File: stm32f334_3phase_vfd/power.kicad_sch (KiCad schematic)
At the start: 4 parts, among them U201 STGIB15CH60TS-L, U202 CC6903SO-x0A, U203 CC6903SO-x0A, U204 CC6903SO-x0A

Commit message: continue schematic work
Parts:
- added C201, C202, C203: 4.7u, symbol Device:C_Small
- added C? (x6): 10p, Capacitor_SMD:C_1206_3216Metric, symbol Device:C_Small
- added C? (x2): 4.7u, Capacitor_SMD:C_1206_3216Metric, symbol Device:C_Small
- added C? (x5): 100n, Capacitor_SMD:C_1206_3216Metric, symbol Device:C_Small
- added C?: 330p, Capacitor_SMD:C_1206_3216Metric, symbol Device:C_Small
- added C?: 1n, Capacitor_SMD:C_1206_3216Metric, symbol Device:C_Small
- added C?: 100n/600V, Capacitor_SMD:C_1206_3216Metric, symbol Device:C_Small
- added J201: TP01, symbol Connector_Generic:Conn_01x01
- added J202: TP02, symbol Connector_Generic:Conn_01x01
- added J203: TP03, symbol Connector_Generic:Conn_01x01
- added J? (x4): TP04, symbol Connector_Generic:Conn_01x01
- added R?: 0.050, symbol Device:R_Small
- added R? (x2): 10k, symbol Device:R_Small
- added R? (x6): 1k, Resistor_SMD:R_1206_3216Metric, symbol Device:R_Small
- added R? (x6): 10k, Resistor_SMD:R_1206_3216Metric, symbol Device:R_Small
- added R?: 1k, symbol Device:R_Small
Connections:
- net at U203.1 (IP+): now also U201.22 (V), U203.2 (IP+), C202.1, J?.1 (Pin_1)
- net OUTPUT_PHB: now reaches U203.3 (IP-)
- net OUTPUT_PHB: now also U203.4 (IP-)
- net GND: now reaches U203.5 (GND)
- net GND: now also U201.16 (GND), U201.9 (GND), U202.5 (GND), U204.5 (GND), C?.1, C?.1, C?.1, C?.1, C?.2, C?.2, C?.2, C?.2, C?.2, C?.2, C?.2, C?.2, C?.2, C?.2, C?.2, C?.2, R?.2, R?.2, R?.2, R?.2, R?.2, R?.2, R?.2, R?.2
- net I_B: now reaches U203.7 (OUT)
- net 3V3_ISENS: now reaches U203.8 (VCC)
- net 3V3_ISENS: now also U202.8 (VCC), U204.8 (VCC), C?.2, C?.2, C?.2
- net lin_u: now reaches U201.10 (LinU)
- net lin_u: now also C?.1, R?.2
- net lin_v: now reaches U201.11 (LinV)
- net lin_v: now also C?.1, R?.2
- net lin_w: now reaches U201.12 (LinW)
- net lin_w: now also C?.1, R?.2
- net VCC_15V: now reaches U201.13 (VccL)
- net VCC_15V: now also U201.8 (VccH), C?.1, C?.1, C?.1, C?.1
- net EM_STOP: now reaches U201.14 (~{SD}/OD)
- net EM_STOP: now also C?.1, R?.1
- net Cin: now reaches U201.15 (Cin)
- net Cin: now also C?.1, J?.1 (Pin_1), R?.1, R?.1
- net Tso: now reaches U201.17 (TSO)
- net N: now reaches U201.18 (NW)
- net N: now also U201.19 (NV), U201.20 (NU), R?.1, R?.2
- net at U201.2 (VbootU): now also C201.2, J201.1 (Pin_1)
- net at U201.21 (W): now also U204.1 (IP+), U204.2 (IP+), C203.1, J?.1 (Pin_1)
- net at U201.23 (U): now also U202.1 (IP+), U202.2 (IP+), C201.1, J?.1 (Pin_1)
- net HV: now reaches U201.24 (P)
- net HV: now also C?.2
- net T2: now reaches U201.25 (T2)
- net T1: now reaches U201.26 (T1)
- net at U201.3 (VbootV): now also C202.2, J202.1 (Pin_1)
- net at U201.4 (VbootW): now also C203.2, J203.1 (Pin_1)
- net hin_u: now reaches U201.5 (HinU)
- net hin_u: now also C?.1, R?.2
- net hin_v: now reaches U201.6 (HinV)
- net hin_v: now also C?.1, R?.2
- net hin_w: now reaches U201.7 (HinW)
- net hin_w: now also C?.1, R?.2
- net OUTPUT_PHC: now reaches U204.3 (IP-)
- net OUTPUT_PHC: now also U204.4 (IP-)
- net I_C: now reaches U204.7 (OUT)
- net OUTPUT_PHA: now reaches U202.3 (IP-)
- net OUTPUT_PHA: now also U202.4 (IP-)
- net I_A: now reaches U202.7 (OUT)
- new net 3V3_DIG: R?.2
- new net HinU: R?.1, R?.1
- new net HinV: R?.1, R?.1
- new net HinW: R?.1, R?.1
- new net LinU: R?.1, R?.1
- new net LinV: R?.1, R?.1
- new net LinW: R?.1, R?.1
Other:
- moved on the sheet: U201, U202, U203, U204

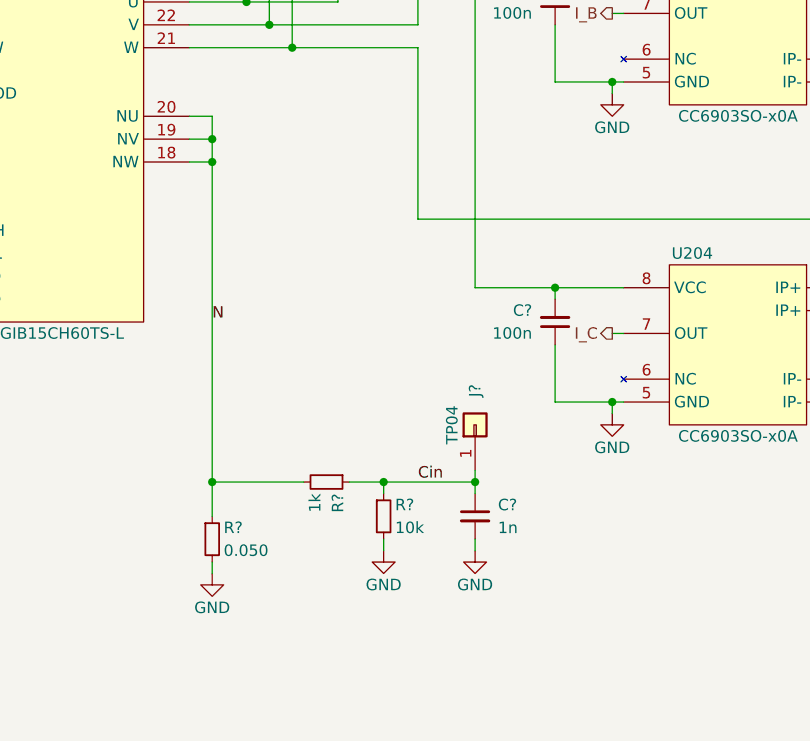
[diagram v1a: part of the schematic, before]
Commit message: update schematic
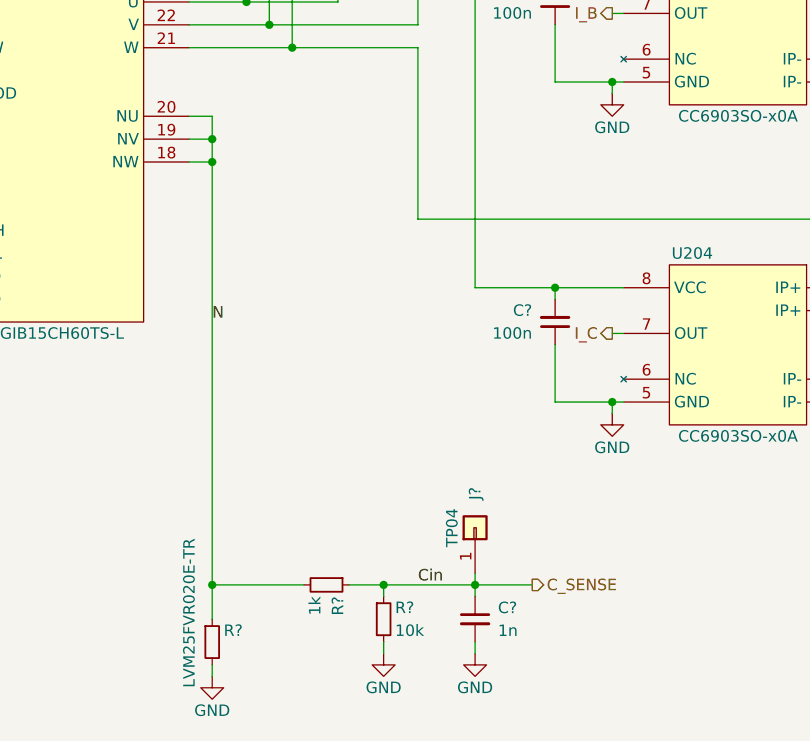
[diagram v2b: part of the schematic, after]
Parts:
- R?: value 0.050 -> LVM25FVR020E-TR; footprint (none) -> Resistor_SMD:R_2512_6332Metric_Pad1.40x3.35mm_HandSolder
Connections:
- net Cin renamed C_SENSE
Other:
- moved on the sheet: C?, J?, R?

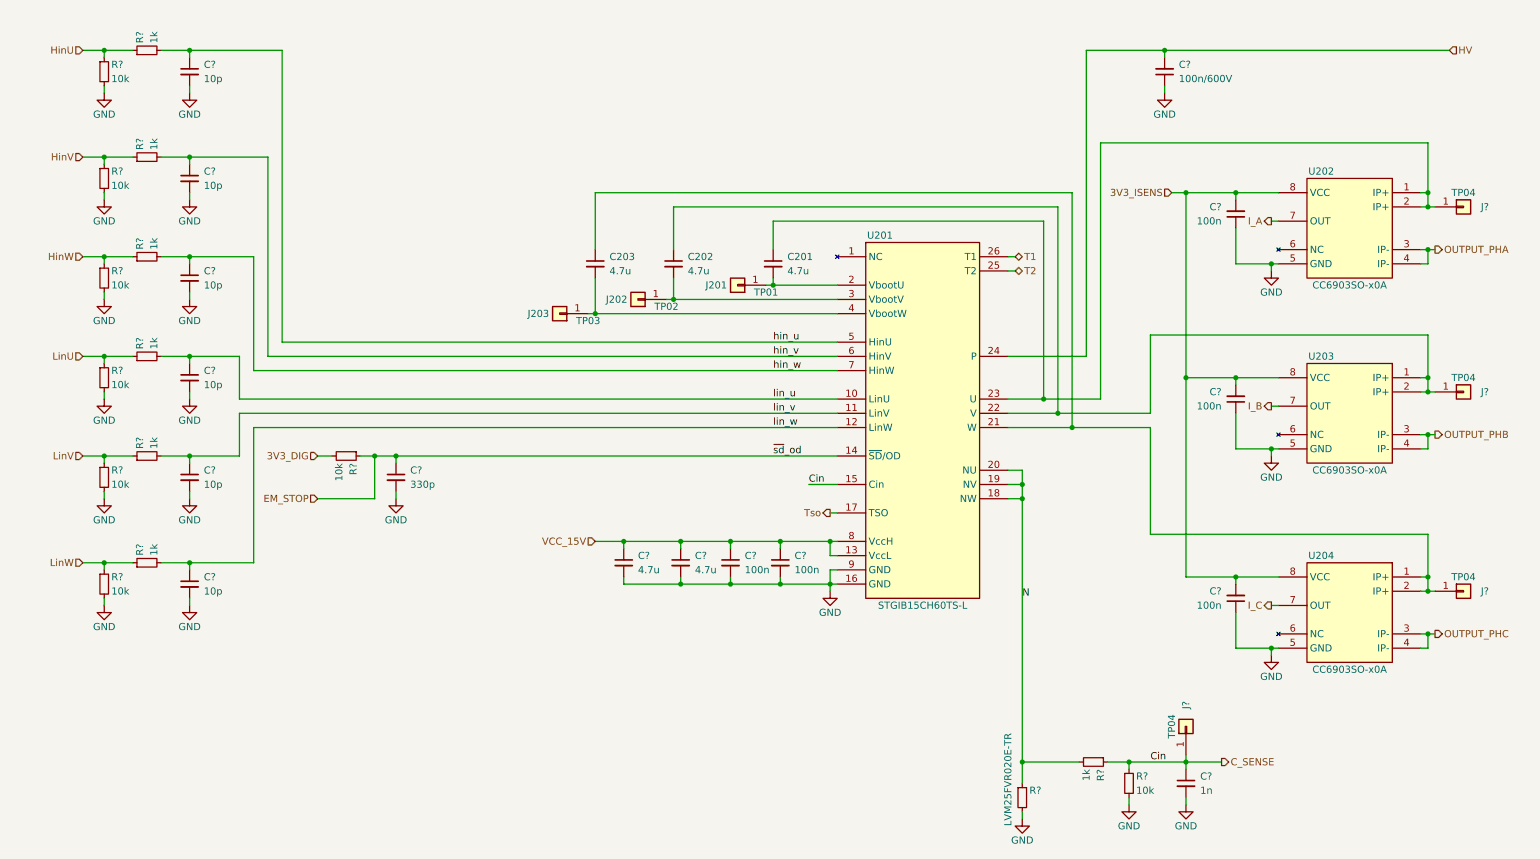
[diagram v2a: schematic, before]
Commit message: update schematic, start power section layout
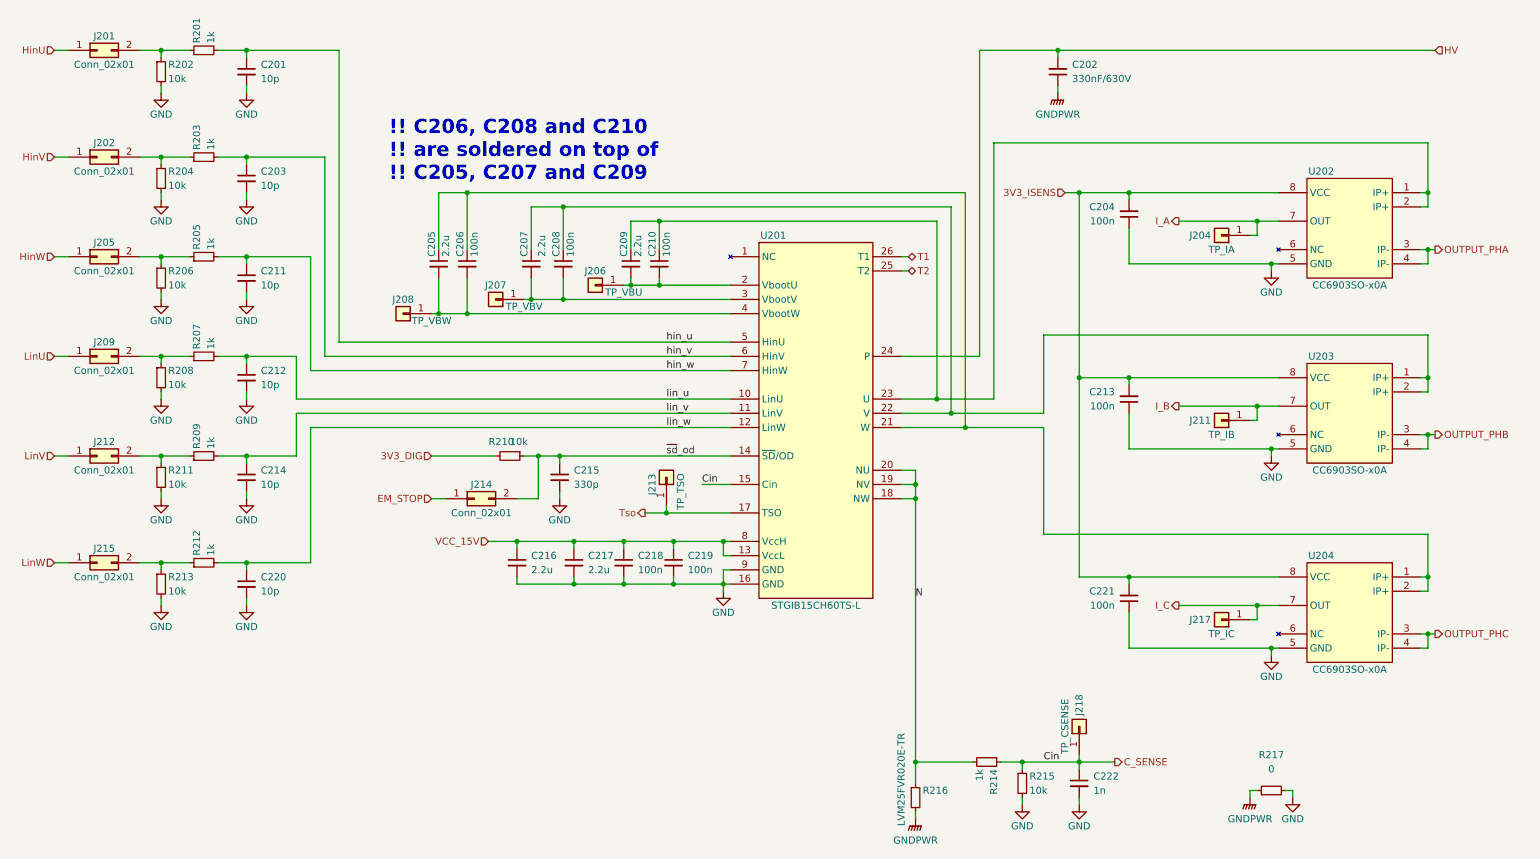
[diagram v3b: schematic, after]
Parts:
- removed J? (x3): TP04, symbol Connector_Generic:Conn_01x01
- added C206, C208, C210: 100n, Capacitor_SMD:C_1206_3216Metric, symbol Device:C_Small
- added J201, J202, J205, J209, J212, J214, J215: Conn_02x01, Connector_PinHeader_2.54mm:PinHeader_2x01_P2.54mm_Vertical, symbol Connector_Generic:Conn_02x01
- added J204: TP_IA, Connector_PinHeader_2.54mm:PinHeader_1x01_P2.54mm_Vertical, symbol Connector_Generic:Conn_01x01
- added J211: TP_IB, Connector_PinHeader_2.54mm:PinHeader_1x01_P2.54mm_Vertical, symbol Connector_Generic:Conn_01x01
- added J213: TP_TSO, Connector_PinHeader_2.54mm:PinHeader_1x01_P2.54mm_Vertical, symbol Connector_Generic:Conn_01x01
- added J217: TP_IC, Connector_PinHeader_2.54mm:PinHeader_1x01_P2.54mm_Vertical, symbol Connector_Generic:Conn_01x01
- added R217: 0, Resistor_SMD:R_0805_2012Metric, symbol Device:R_Small
- C202: renamed from C?; value 100n/600V -> 330nF/630V; footprint Capacitor_SMD:C_1206_3216Metric -> Capacitor_THT:C_Rect_L24.0mm_W10.1mm_P22.50mm_MKT
- C205: renamed from C203; value 4.7u -> 2.2u; footprint (none) -> Capacitor_SMD:C_1206_3216Metric
- C207: renamed from C202; value 4.7u -> 2.2u; footprint (none) -> Capacitor_SMD:C_1206_3216Metric
- C209: renamed from C201; value 4.7u -> 2.2u; footprint (none) -> Capacitor_SMD:C_1206_3216Metric
- C216, C217: renamed from C?; value 4.7u -> 2.2u
- J206: renamed from J201; value TP01 -> TP_VBU; footprint (none) -> Connector_PinHeader_2.54mm:PinHeader_1x01_P2.54mm_Vertical
- J207: renamed from J202; value TP02 -> TP_VBV; footprint (none) -> Connector_PinHeader_2.54mm:PinHeader_1x01_P2.54mm_Vertical
- J208: renamed from J203; value TP03 -> TP_VBW; footprint (none) -> Connector_PinHeader_2.54mm:PinHeader_1x01_P2.54mm_Vertical
- J218: renamed from J?; value TP04 -> TP_CSENSE; footprint (none) -> Connector_PinHeader_2.54mm:PinHeader_1x01_P2.54mm_Vertical
- R210, R214, R215: renamed from R?; footprint (none) -> Resistor_SMD:R_1206_3216Metric
- U201: footprint (none) -> stm32f334_3phase_vfd:SDIP2B-26L_L1_STM
- gave numbers to parts that had none: 26
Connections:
- net EM_STOP: now also J214.1 (Pin_1); no longer C215.1, R210.1, U201.14 (~{SD}/OD)
- net GND: now also R217.2; no longer C202.1, R216.2
- net HinU: now also J201.1 (Pin_1); no longer R201.1, R202.1
- net HinV: now also J202.1 (Pin_1); no longer R203.1, R204.1
- net HinW: now also J205.1 (Pin_1); no longer R205.1, R206.1
- net I_A: now also J204.1 (Pin_1)
- net I_B: now also J211.1 (Pin_1)
- net I_C: now also J217.1 (Pin_1)
- net LinU: now also J209.1 (Pin_1); no longer R207.1, R208.1
- net LinV: now also J212.1 (Pin_1); no longer R209.1, R211.1
- net LinW: now also J215.1 (Pin_1); no longer R212.1, R213.1
- net Tso: now also J213.1 (Pin_1)
- net at C207.1, U201.22 (V), U203.1 (IP+)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: now also C208.1
- net at C207.2, J207.1 (Pin_1), U201.3 (VbootV): now also C208.2
- net at C205.1, U201.21 (W), U204.1 (IP+)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: now also C206.1
- net at C205.2, J208.1 (Pin_1), U201.4 (VbootW): now also C206.2
- net at C209.2, J206.1 (Pin_1), U201.2 (VbootU): now also C210.2
- net at C209.1, U201.23 (U), U202.1 (IP+)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: now also C210.1
- new net: J209.2 (Pin_2), R207.1, R208.1
- new net: J202.2 (Pin_2), R203.1, R204.1
- new net: J201.2 (Pin_2), R201.1, R202.1
- new net: J205.2 (Pin_2), R205.1, R206.1
- new net: J215.2 (Pin_2), R212.1, R213.1
- new net: J212.2 (Pin_2), R209.1, R211.1
- new net GNDPWR: C202.1, R216.2, R217.1
- new net ~{sd}_od: C215.1, J214.2 (Pin_2), R210.1, U201.14 (~{SD}/OD)
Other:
- note added: "!! C206, C208 and C210 !! are soldered on top of !! C205, C207 and C209"
- moved on the sheet: C201, C202, C203, C204, C205, C207, C209, C211, C212, C213, C214, C215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

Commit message: move 3 phase current sensors on a new board, allow for the current sense board to be stacked
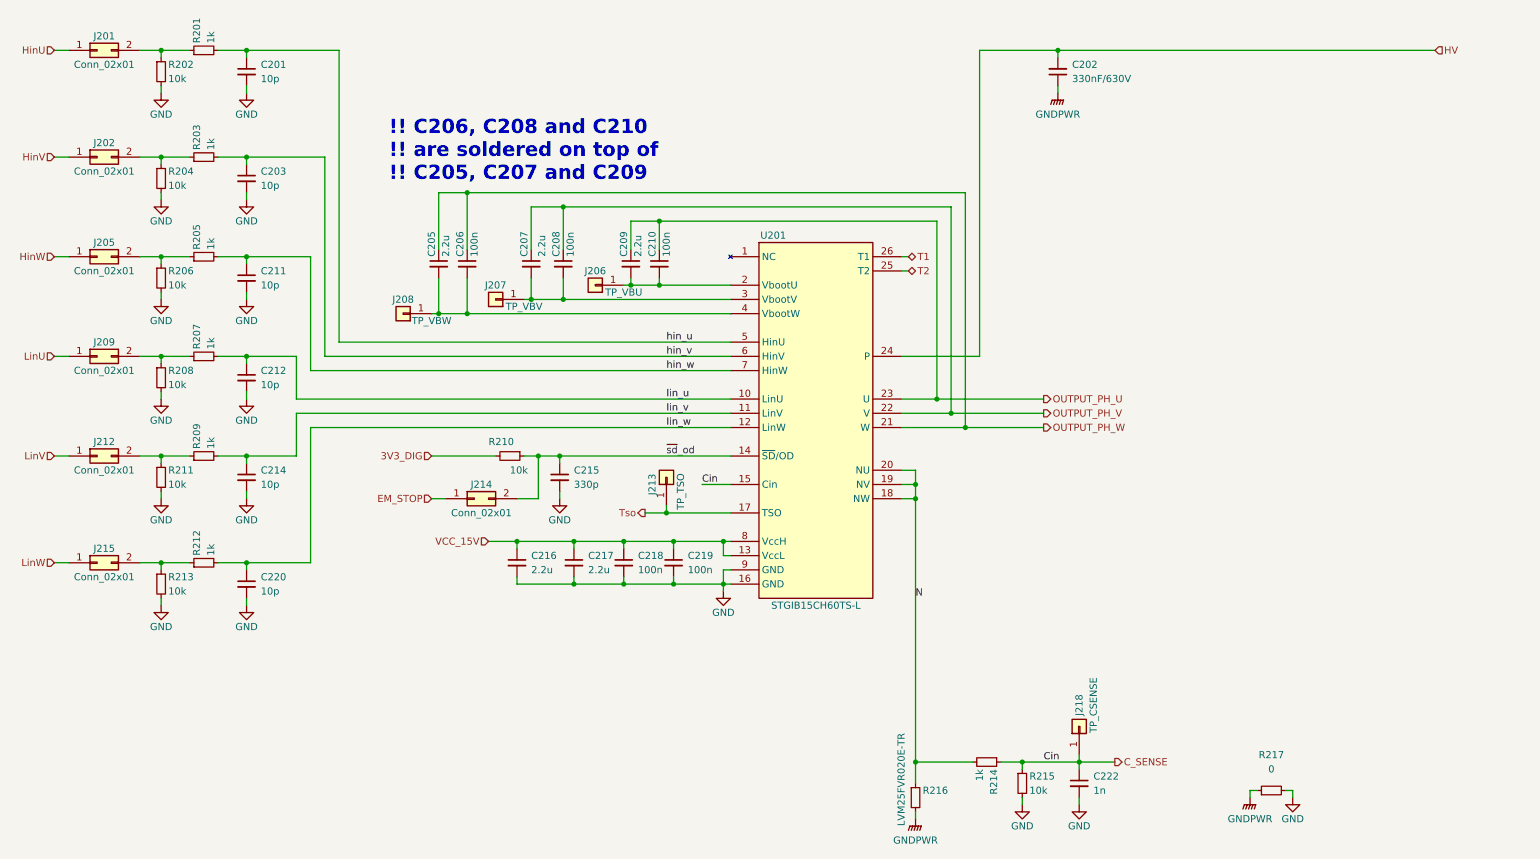
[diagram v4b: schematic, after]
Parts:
- removed C204, C213, C221: 100n, Capacitor_SMD:C_1206_3216Metric, symbol Device:C_Small
- removed J204: TP_IA, Connector_PinHeader_2.54mm:PinHeader_1x01_P2.54mm_Vertical, symbol Connector_Generic:Conn_01x01
- removed J211: TP_IB, Connector_PinHeader_2.54mm:PinHeader_1x01_P2.54mm_Vertical, symbol Connector_Generic:Conn_01x01
- removed J217: TP_IC, Connector_PinHeader_2.54mm:PinHeader_1x01_P2.54mm_Vertical, symbol Connector_Generic:Conn_01x01
- removed U202, U203, U204: CC6903SO-x0A, Package_SO:SO-8_3.9x4.9mm_P1.27mm, symbol custom_parts:CC6903SO-x0A
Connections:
- net OUTPUT_PH_U: now reaches C209.1, C210.1, U201.23 (U)
- net OUTPUT_PH_V: now reaches C207.1, C208.1, U201.22 (V)
- net OUTPUT_PH_W: now reaches C205.1, C206.1, U201.21 (W)

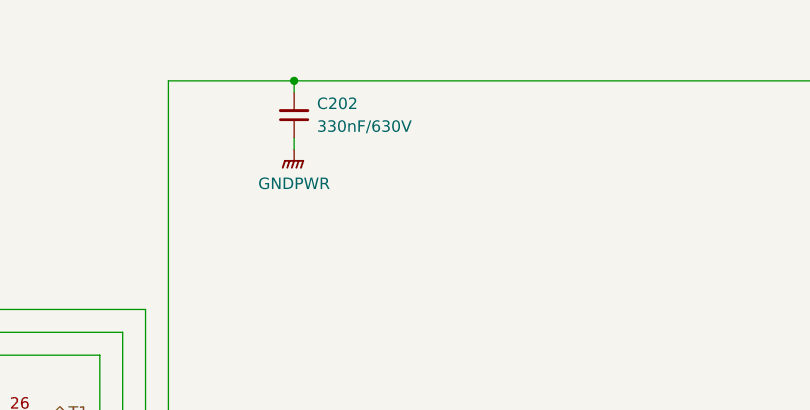
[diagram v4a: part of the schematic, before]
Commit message: switch to LQFP48 cpu, continue workin on layout
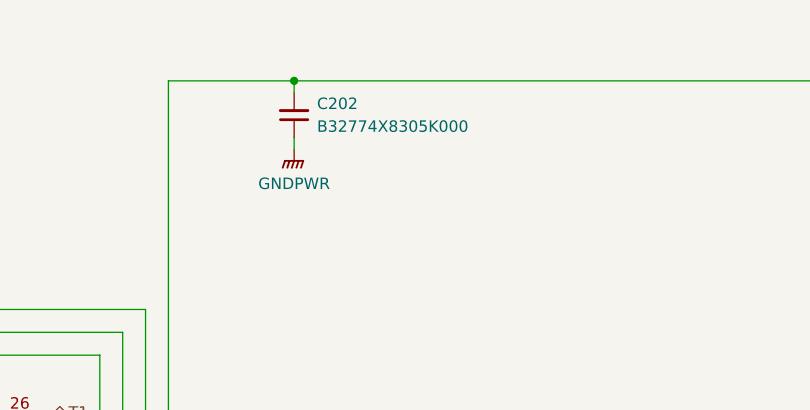
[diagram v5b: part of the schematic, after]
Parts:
- C202: value 330nF/630V -> B32774X8305K000; footprint Capacitor_THT:C_Rect_L24.0mm_W10.1mm_P22.50mm_MKT -> Capacitor_THT:C_Rect_L31.5mm_W11.0mm_P27.50mm_MKS4
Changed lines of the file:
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@@
       (effects (font (size 1.27 1.27)) (justify right))
     )
-    (property "Value" "330nF/630V" (id 1) (at 201.93 25.3935 0)
+    (property "Value" "B32774X8305K000" (id 1) (at 201.93 25.3935 0)
       (effects (font (size 1.27 1.27)) (justify right))
     )
-    (property "Footprint" "Capacitor_THT:C_Rect_L24.0mm_W10.1mm_P22.50mm_MKT" (id 2) (at 199.39 24.13 0)
+    (property "Footprint" "Capacitor_THT:C_Rect_L31.5mm_W11.0mm_P27.50mm_MKS4" (id 2) (at 199.39 24.13 0)
       (effects (font (size 1.27 1.27)) hide)
     )
